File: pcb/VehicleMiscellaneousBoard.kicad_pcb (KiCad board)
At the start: 4 copper layers, 50 x 50 mm, 1 part

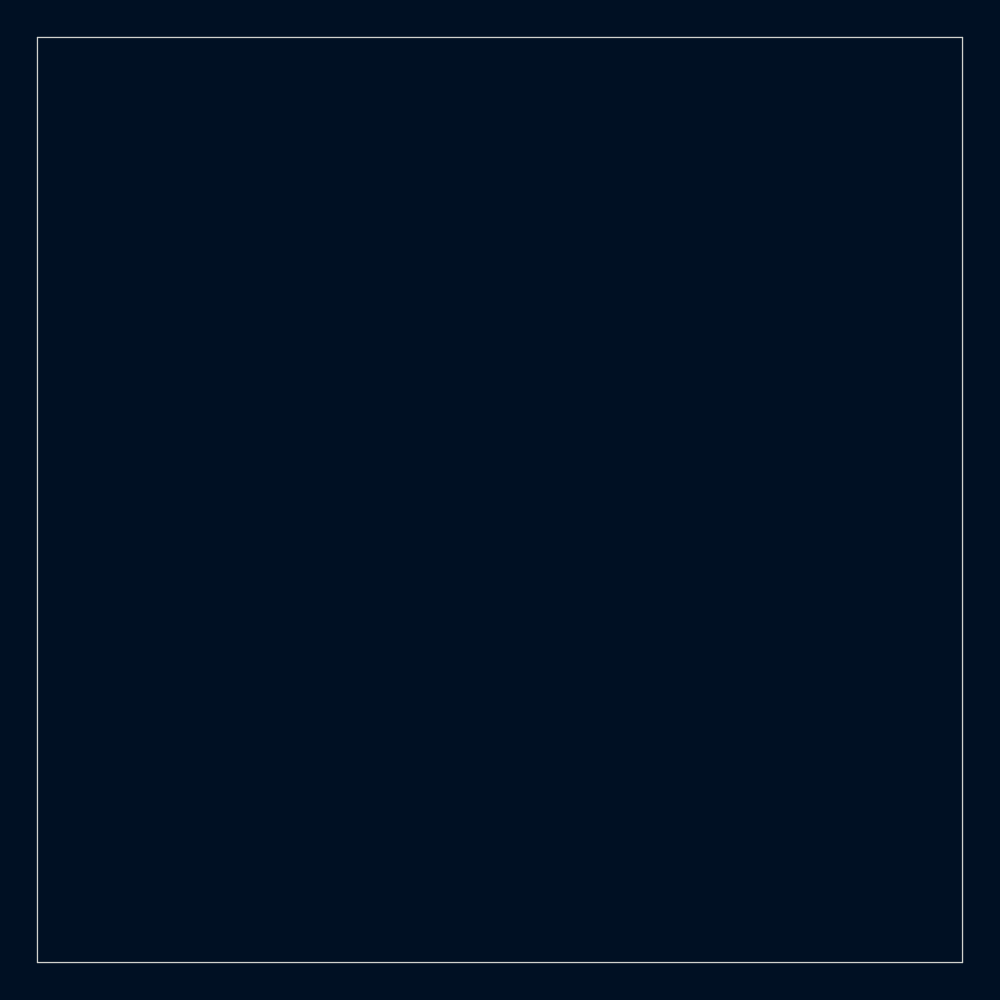
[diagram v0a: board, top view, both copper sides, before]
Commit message: Made footprint for OpenMV H7+.
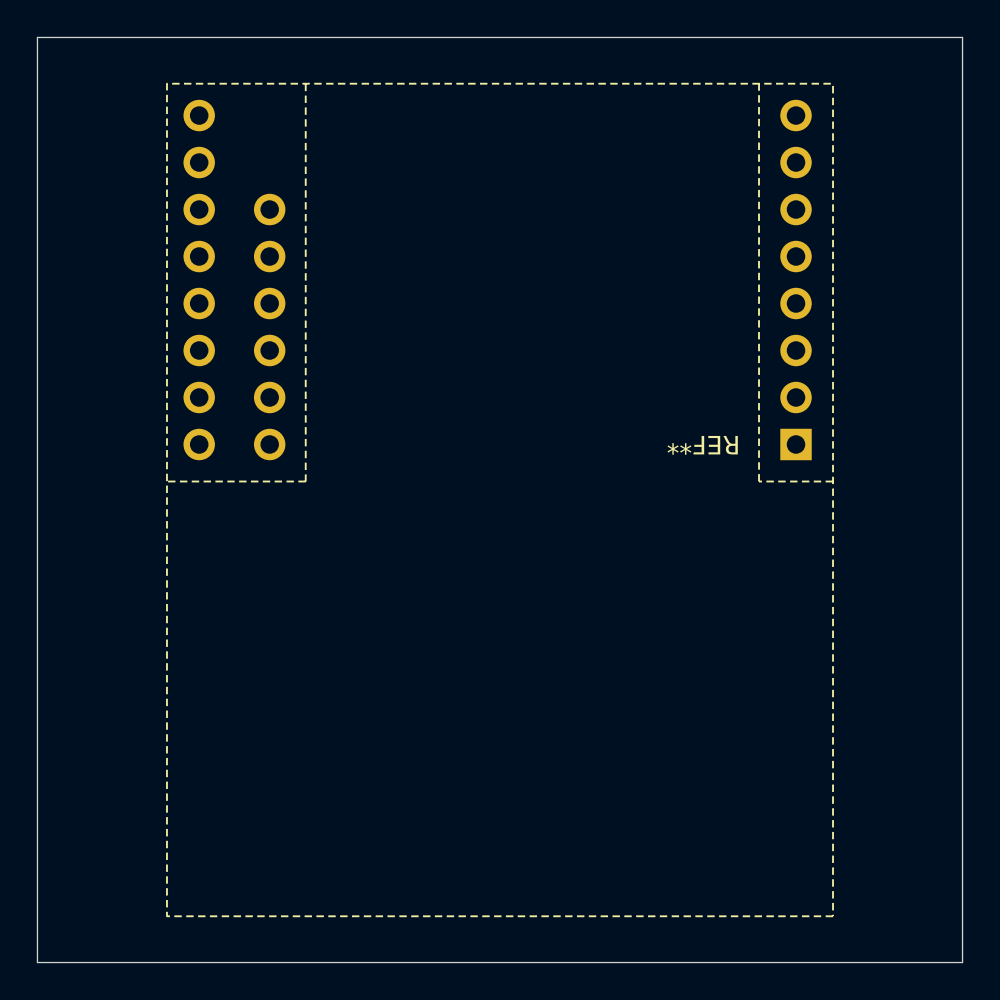
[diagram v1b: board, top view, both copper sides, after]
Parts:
- added REF**: OpenMV_H7_Plus, pcb:OpenMV_H7_Plus, F.Cu at (166.0, 97.0)

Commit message: Made symbol for OpenMV H7+.
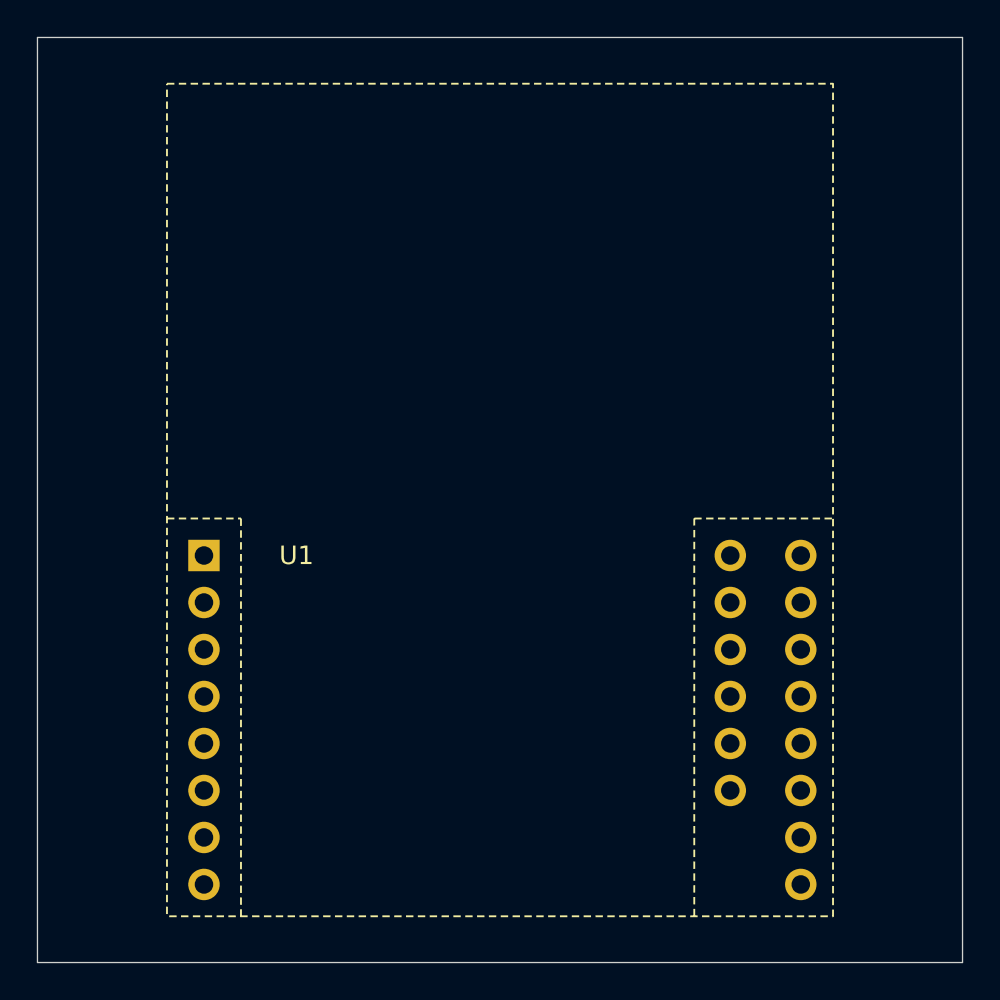
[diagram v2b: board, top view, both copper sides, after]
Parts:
- removed REF**: OpenMV_H7_Plus, pcb:OpenMV_H7_Plus
- added U1: OpenMV H7+, pcb:OpenMV_H7_Plus, F.Cu at (134.0, 103.0)

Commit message: Added stack connector and XIAO ESP32 to `VehicleMiscellaneousBoard`.
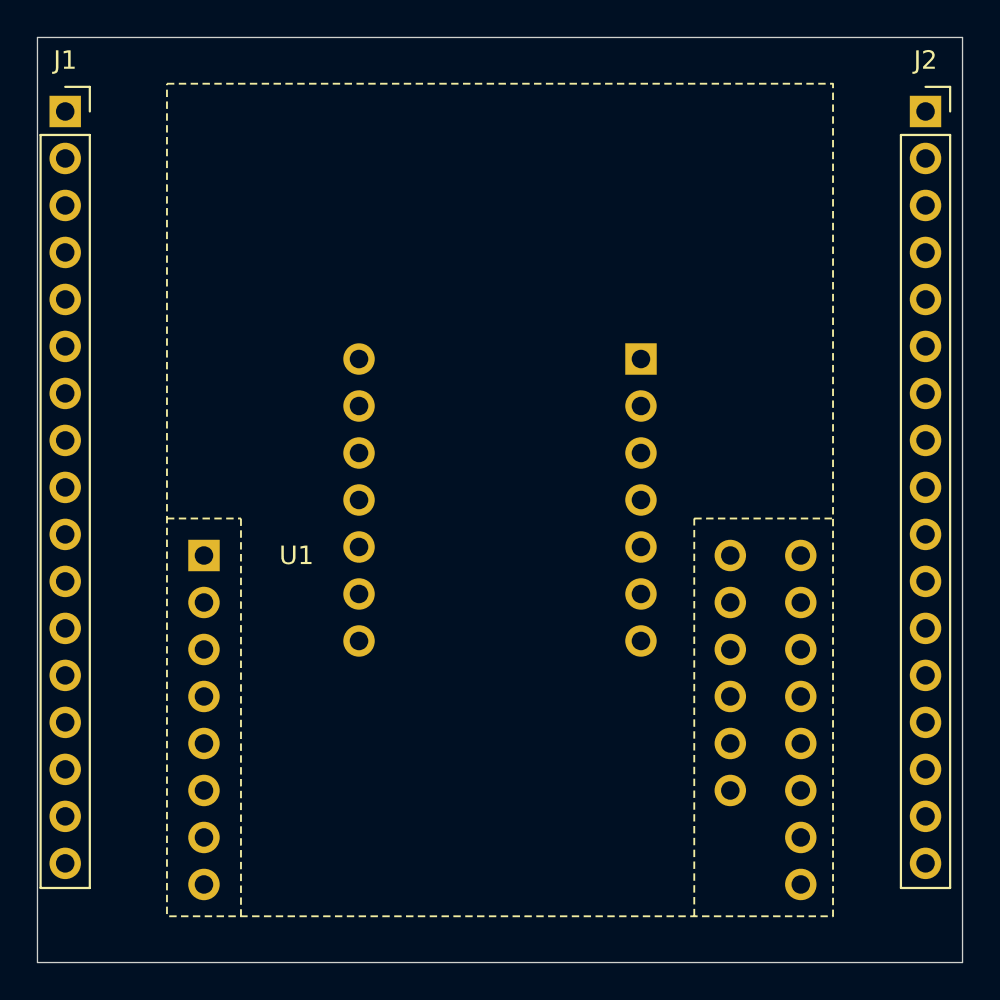
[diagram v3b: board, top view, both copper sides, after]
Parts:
- added J1: Conn_01x17, Connector_PinSocket_2.54mm:PinSocket_1x17_P2.54mm_Vertical, F.Cu at (126.5, 79.0)
- added J2: Conn_01x17, Connector_PinSocket_2.54mm:PinSocket_1x17_P2.54mm_Vertical, F.Cu at (173.0, 79.0)
- added U2: Seeed_Studio_XIAO-ESP32-S3-Sense, pcb:Seeed_Studio_XIAO_ESP32_S3, B.Cu at (150.0, 100.0)
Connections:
- U1 pad +3.3V: unconnected-(U1-Pad+3.3V) -> +3.3V
- U1 pad GND: unconnected-(U1-PadGND) -> GND

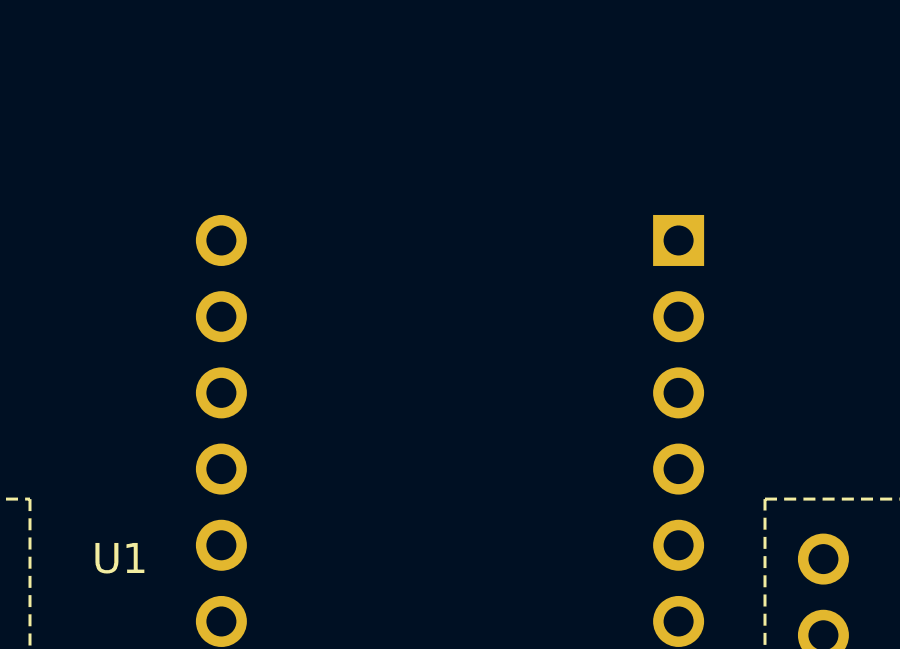
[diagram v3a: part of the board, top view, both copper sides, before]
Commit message: Updated symbol and footprint of the XIAO ESP32 to account for the under pads.
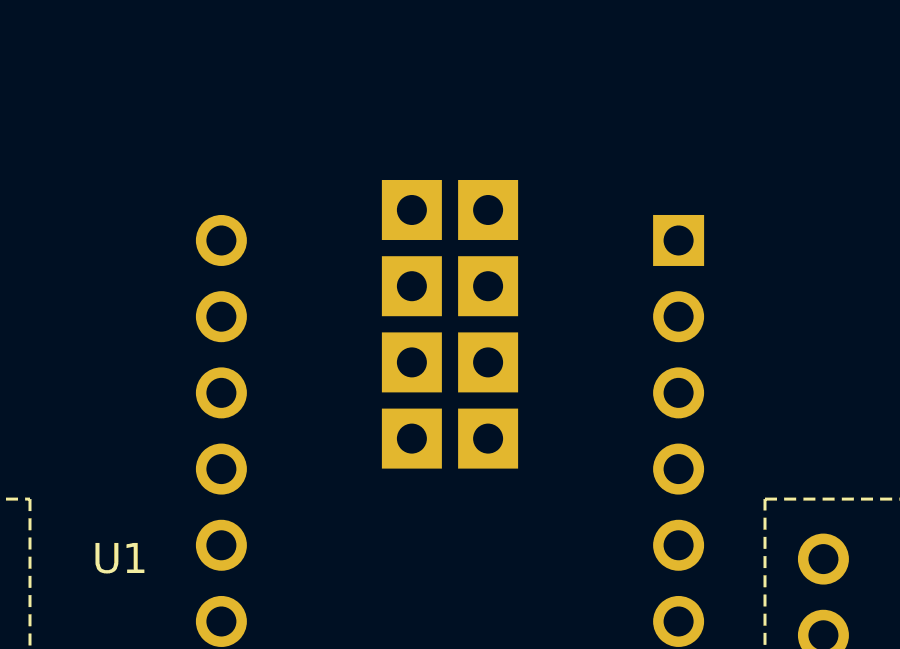
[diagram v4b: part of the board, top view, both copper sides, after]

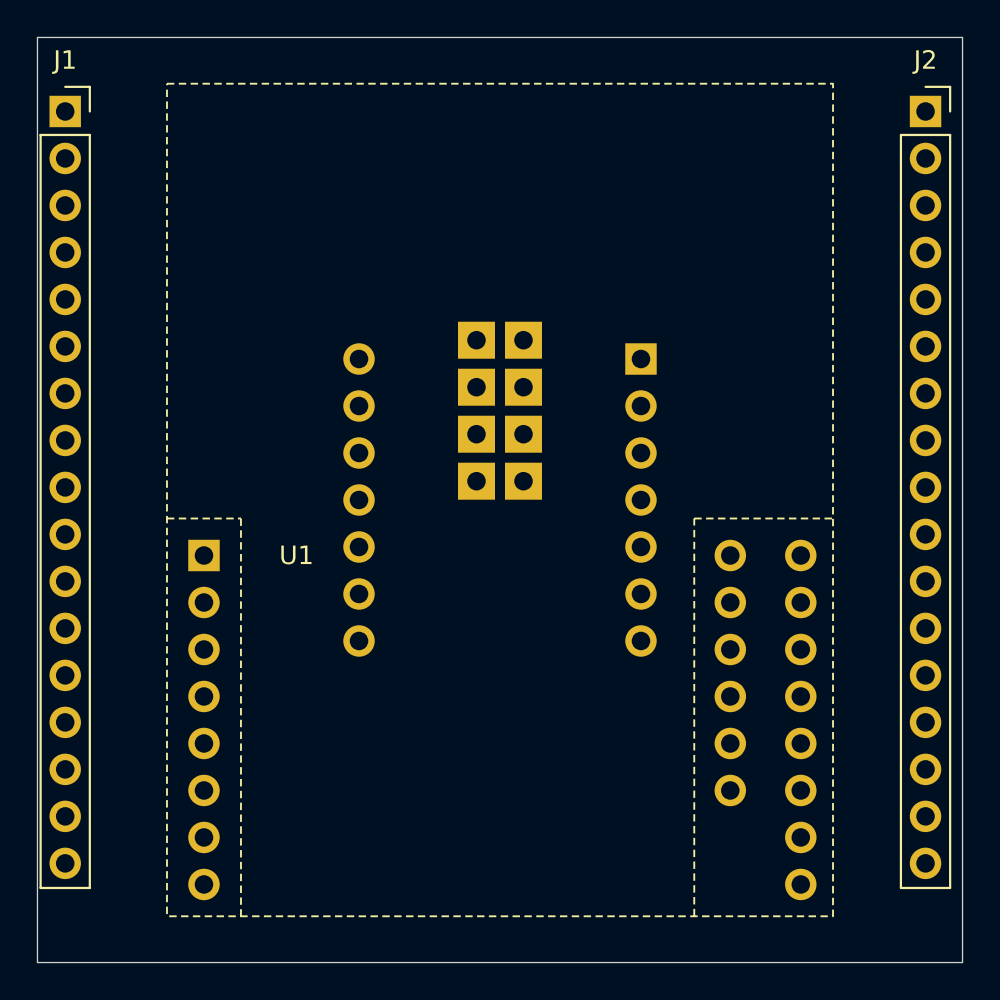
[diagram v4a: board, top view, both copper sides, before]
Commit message: Made `VehicleMiscellaneousBoard` switch to using the vehicle stack connector.
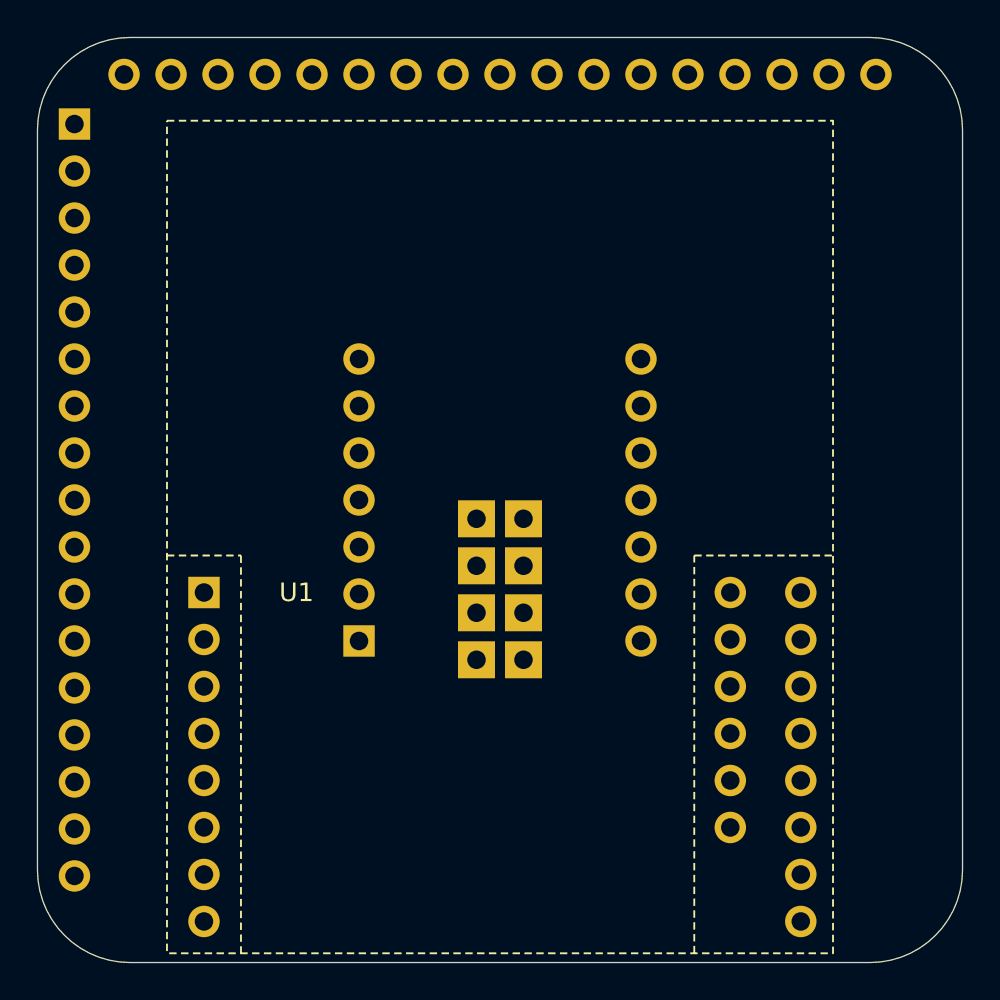
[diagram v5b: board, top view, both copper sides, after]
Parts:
- removed J1, J2: Conn_01x17, Connector_PinSocket_2.54mm:PinSocket_1x17_P2.54mm_Vertical
- added J6: ~, pcb:VehicleStackConnector, F.Cu at (150.0, 100.0)
- moved U1 2.00 mm to (134.0, 105.0)
- turned U2 to 0 degrees
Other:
- outline, holes or cut-outs redrawn
